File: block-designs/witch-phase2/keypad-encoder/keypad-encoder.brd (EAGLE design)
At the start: 160 x 100 mm, 70 parts, among them IC1 74AHC1G14DBV, IC2 74AHC1G14DBV, IC3 74AHC1G14DBV, IC4 74AHC1G14DBV, IC5 74AHC1G14DBV

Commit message: completed schematic with basic pcb layout
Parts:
- removed D26, D28, D30, D31, D32, D33, D34: (no value), SparkFun-DiscreteSemi:DIODE-1N4001
- removed JP1: (no value), pinhead:1X18
- added D1, D2: (no value), SparkFun-DiscreteSemi:DIODE-1N4001
- added IC6: 74LVC1G17DBV, 74xx-little-us:SOT23-5
- added IC7: 74LVC1G14DBV, 74xx-little-us:SOT23-5
- added JP2: (no value), pinhead:1X10
- added JP3: (no value), pinhead:1X18
- added R17, R18, R19, R20, R21: 1k, resistor:R0805
- C1, C10, C11, C12, C13, C14, C15, C16, C2, C3, C4, C5, C6, C7, C8, C9: value 10uF -> 0.1uF
- IC1, IC2, IC3, IC4, IC5: value 74AHC1G14DBV -> 74LVC1G17DBV
- R1, R10, R11, R12, R13, R14, R15, R16, R2, R3, R4, R5, R6, R7, R8, R9: value 10k -> 1k
- moved D23 353.3 mm to (139.7, 35.6), turned to 90 degrees
- moved D25 352.2 mm to (129.5, 35.6), turned to 90 degrees
- moved D24 348.5 mm to (143.5, 35.6), turned to 90 degrees
- moved D27 337.5 mm to (88.9, 35.6), turned to 90 degrees
- moved D19 323.8 mm to (99.1, 35.6), turned to 90 degrees
- moved D20 319.8 mm to (102.9, 35.6), turned to 90 degrees
- moved D29 317.3 mm to (8.89, 35.6), turned to 90 degrees
- moved D14 309.0 mm to (113.0, 35.6), turned to 90 degrees
- moved D21 308.1 mm to (48.3, 35.6), turned to 90 degrees
- moved D22 305.2 mm to (52.1, 35.6), turned to 90 degrees
- moved D18 303.5 mm to (62.2, 35.6), turned to 90 degrees
- moved D13 302.6 mm to (109.2, 35.6), turned to 90 degrees
- moved D17 297.4 mm to (58.4, 35.6), turned to 90 degrees
- moved D8 289.8 mm to (123.2, 35.6), turned to 90 degrees
- moved D7 283.5 mm to (119.4, 35.6), turned to 90 degrees
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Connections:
- removed net N$10: JP1.9
- removed net N$11: JP1.10
- removed net N$12: JP1.11
- removed net N$13: JP1.12
- removed net N$14: JP1.13
- removed net N$15: JP1.14
- removed net N$16: JP1.15
- removed net N$17: JP1.16
- removed net N$18: JP1.17
- removed net N$2: JP1.1
- removed net N$20: R1.1, R10.1, R11.1, R12.1, R13.1, R14.1, R15.1, R16.1, R2.1, R3.1, R4.1, R5.1, R6.1, R7.1, R8.1, R9.1
- removed net N$3: JP1.2
- removed net N$31: C11.1, D23.A, D24.A, R11.2
- removed net N$37: D11.C, D13.C, D15.C, D17.C, D19.C, D21.C, D23.C, D25.C, D27.C, D29.C, D3.C, D31.C, D33.C, D5.C, D7.C, D9.C
- removed net N$38: D10.C, D12.C, D14.C, D16.C, D18.C, D20.C, D22.C, D24.C, D26.C, D28.C, D30.C, D32.C, D34.C, D4.C, D6.C, D8.C
- removed net N$4: JP1.3
- removed net N$5: JP1.4
- removed net N$6: JP1.5
- removed net N$7: JP1.6
- removed net N$8: JP1.7
- removed net N$9: JP1.8
- new net !RESET: IC7.4, JP2.8
- new net EXEC: IC6.4, JP2.9
- new net OUT_A: D1.C, D15.C, D17.C, D21.C, D29.C, D3.C, IC1.2, R17.2
- new net OUT_B: D19.C, D22.C, D5.C, D7.C, IC2.2, R18.2
- new net OUT_C: D11.C, D23.C, D25.C, D4.C, D6.C, D9.C, IC3.2, R19.2
- new net OUT_D: D10.C, D13.C, D16.C, D24.C, D8.C, IC4.2, R20.2
- new net OUT_E: D12.C, D14.C, D18.C, D2.C, D20.C, D27.C, IC5.2, R21.2
- new net SIGA: IC1.4, JP2.2
- new net SIGB: IC2.4, JP2.3
- new net SIGC: IC3.4, JP2.4
- new net SIGD: IC4.4, JP2.5
- new net SIGE: IC5.4, JP2.6
- new net SW-EXEC: JP3.15, R15.1
- new net SW-MINUS: JP3.10, R13.1
- new net SW-ORDER: JP3.17, R11.1
- new net SW-PLUS: JP3.2, R14.1
- new net SW-RESET: JP3.14, R16.1
- new net SW-SPACE: JP3.16, R12.1
- new net SW0: JP3.6, R10.1
- new net SW1: JP3.5, R6.1
- new net SW2: JP3.9, R1.1
- new net SW3: JP3.13, R2.1
- new net SW4: JP3.4, R3.1
- new net SW5: JP3.8, R4.1
- new net SW6: JP3.12, R5.1
- new net SW7: JP3.3, R7.1
- new net SW8: JP3.7, R8.1
- new net SW9: JP3.11, R9.1
- net GND: now also IC6.3, IC7.3, JP2.10, JP3.18, R17.1, R18.1, R19.1, R20.1, R21.1
- net N$1: now also C11.1, D1.A, D2.A, D23.A, D24.A, R11.2; no longer JP1.18
- net N$32: no longer D26.A
- net N$33: no longer D28.A
- net N$34: no longer D30.A
- net N$35: now also IC6.2; no longer D31.A, D32.A
- net N$36: now also IC7.2; no longer D33.A, D34.A
- net VCC: now also IC6.5, IC7.5, JP2.1, JP3.1
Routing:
- net N$1: track 0.00 -> 19.4 mm
- net N$30: track 0.00 -> 11.8 mm
- net N$29: track 0.00 -> 11.8 mm
- net N$26: track 0.00 -> 11.8 mm
- net N$25: track 0.00 -> 11.8 mm
- net N$23: track 0.00 -> 11.8 mm
- net N$22: track 0.00 -> 11.8 mm
- net N$27: track 0.00 -> 11.7 mm
- net N$24: track 0.00 -> 11.7 mm
- net N$28: track 0.00 -> 11.7 mm
- net N$19: track 0.00 -> 11.7 mm
- net N$36: track 0.00 -> 11.7 mm
- net N$35: track 0.00 -> 11.7 mm
- net N$32: track 0.00 -> 7.94 mm
- net N$34: track 0.00 -> 7.94 mm
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- added copper zone on layer 1, net GND
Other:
- board size 160 x 100 mm -> 159.8 x 99.8 mm

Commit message: layout cleanup
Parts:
- moved IC1 8.13 mm to (53.3, 77.0)
- moved IC2 8.13 mm to (62.2, 77.0)
- moved IC3 8.13 mm to (71.1, 77.0)
- moved IC4 8.13 mm to (80.0, 77.0)
- moved IC5 8.13 mm to (88.9, 77.0)
- moved IC6 8.13 mm to (106.7, 77.0)
- moved IC7 8.13 mm to (97.8, 77.0)
- moved R17 8.13 mm to (52.1, 69.3)
- moved R18 8.13 mm to (61.0, 69.3)
- moved R19 8.13 mm to (69.8, 69.3)
- moved R20 8.13 mm to (78.7, 69.3)
- moved R21 8.13 mm to (87.6, 69.3)
- moved C15 5.59 mm to (110.5, 69.3)
- moved C16 5.59 mm to (101.6, 69.3)
- moved R15 5.59 mm to (106.7, 69.3)
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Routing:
- net OUT_A: track 6.46 -> 243.1 mm, vias 0 -> 7
- net OUT_D: track 6.46 -> 205.4 mm, vias 0 -> 6
- net OUT_C: track 6.46 -> 201.1 mm, vias 0 -> 7
- net OUT_E: track 6.46 -> 162.0 mm, vias 0 -> 6
- net OUT_B: track 6.46 -> 128.2 mm, vias 0 -> 5
- net SW-PLUS: track 0.00 -> 75.5 mm
- net SW-EXEC: track 0.00 -> 73.7 mm, vias 0 -> 1
- net SW7: track 0.00 -> 68.2 mm
- net SW-RESET: track 0.00 -> 67.8 mm, vias 0 -> 1
- net SW-ORDER: track 0.00 -> 63.1 mm
- net SW4: track 0.00 -> 60.3 mm
- net SW-SPACE: track 0.00 -> 55.6 mm
- net SW3: track 0.00 -> 53.1 mm
- net SW1: track 0.00 -> 52.8 mm
- net SW0: track 0.00 -> 44.8 mm
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- added copper zone on layer 16, net VCC

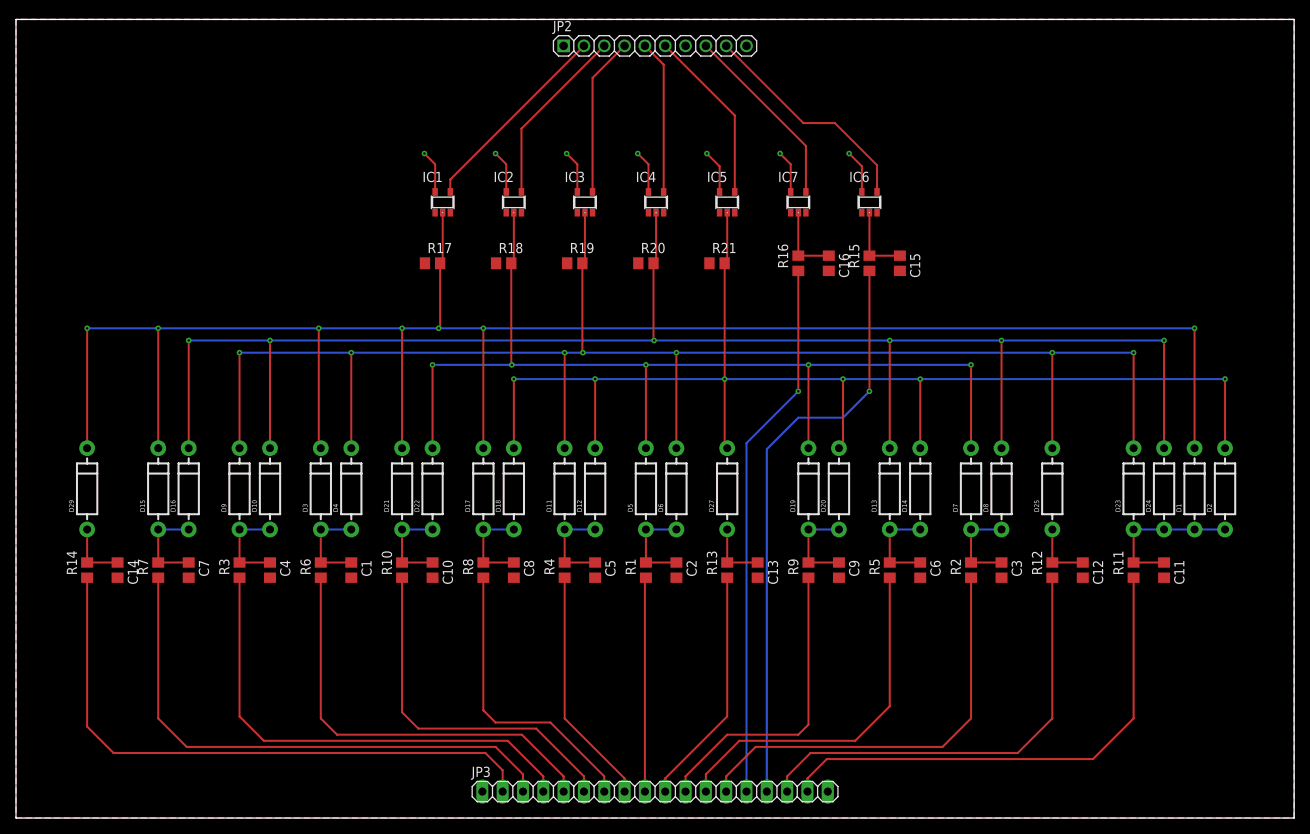
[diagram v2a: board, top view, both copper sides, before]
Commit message: reduced size of module and layout cleanup
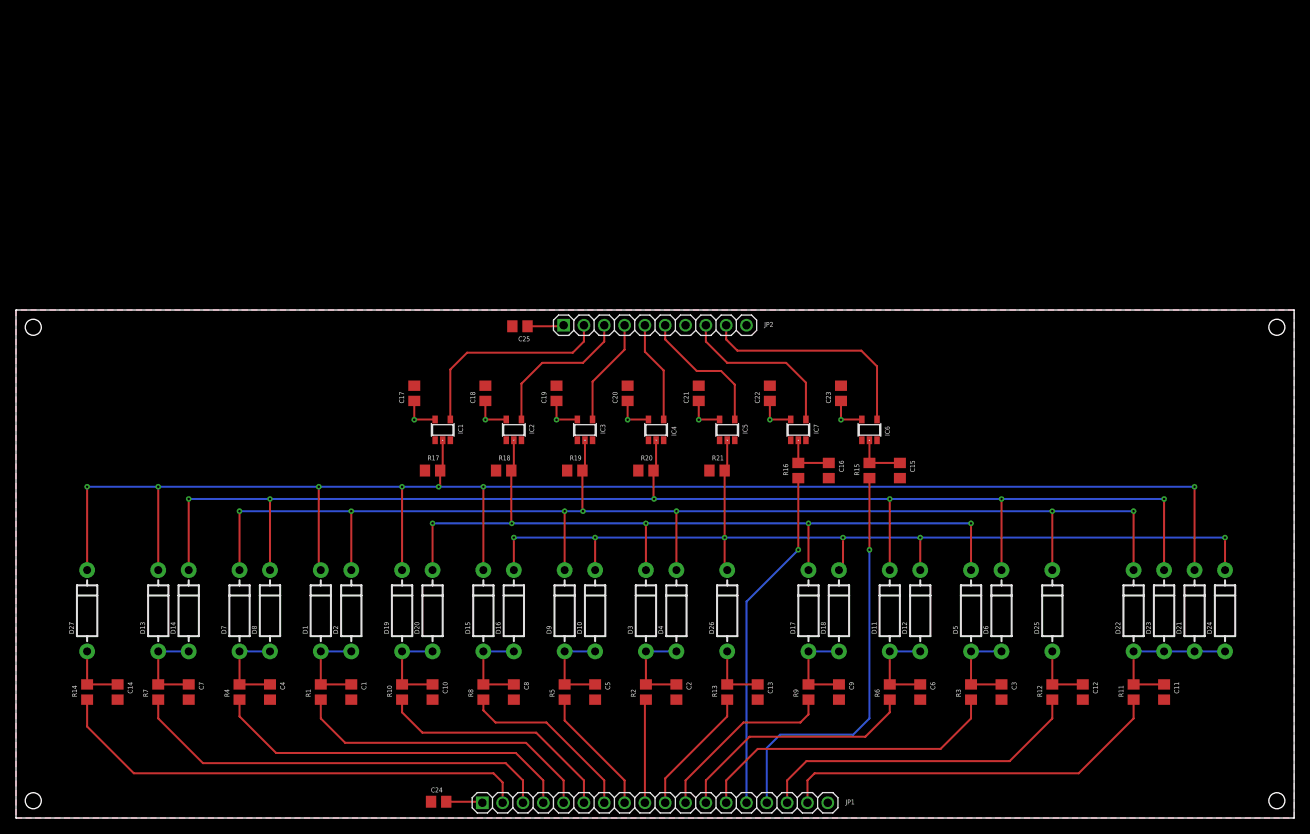
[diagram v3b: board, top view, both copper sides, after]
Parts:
- removed D29: (no value), SparkFun-DiscreteSemi:DIODE-1N4001
- removed JP3: (no value), pinhead:1X18
- added C17, C18, C19, C20, C21, C22, C23: 0.1uF, resistor:C0805
- added C24: 1uF, resistor:C0805
- added C25: 10uF, resistor:C0805
- added D26: (no value), SparkFun-DiscreteSemi:DIODE-1N4001
- added JP1: (no value), pinhead:1X18
- moved D1 110.3 mm to (38.1, 25.9)
- moved D2 110.3 mm to (41.9, 25.9)
- moved D21 100.2 mm to (147.3, 25.9)
- moved D13 92.7 mm to (17.8, 25.9)
- moved D14 92.7 mm to (21.6, 25.9)
- moved D7 92.7 mm to (27.9, 25.9)
- moved D8 92.7 mm to (31.8, 25.9)
- moved R3 92.7 mm to (119.4, 15.7)
- moved D22 88.9 mm to (139.7, 25.9)
- moved D27 81.4 mm to (8.89, 25.9)
- moved R6 72.7 mm to (109.2, 15.7)
- moved D19 53.0 mm to (48.3, 25.9)
- moved D20 53.0 mm to (52.1, 25.9)
- moved D18 43.4 mm to (102.9, 25.9)
- moved D10 43.4 mm to (72.4, 25.9)
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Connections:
- net GND: now also C17.2, C18.2, C19.2, C20.2, C21.2, C22.2, C23.2, C24.2, C25.2, JP1.18; no longer JP3.18
- net N$1: now also D21.A, D22.A; no longer D1.A, D2.A
- net N$19: now also D1.A, D2.A, R1.2; no longer D3.A, D4.A, R6.2
- net N$22: now also D3.A, D4.A, R2.2; no longer D5.A, D6.A, R1.2
- net N$23: now also D5.A, D6.A, R3.2; no longer D7.A, D8.A, R2.2
- net N$24: now also D7.A, D8.A, R4.2; no longer D10.A, D9.A, R3.2
- net N$25: now also D10.A, D9.A, R5.2; no longer D11.A, D12.A, R4.2
- net N$26: now also D11.A, D12.A, R6.2; no longer D13.A, D14.A, R5.2
- net N$27: now also D13.A, D14.A; no longer D15.A, D16.A
- net N$28: now also D15.A, D16.A; no longer D17.A, D18.A
- net N$29: now also D17.A, D18.A; no longer D19.A, D20.A
- net N$30: now also D19.A, D20.A; no longer D21.A, D22.A
- net N$33: now also D26.A; no longer D27.A
- net N$34: now also D27.A; no longer D29.A
- net OUT_A: now also D13.C, D19.C, D27.C; no longer D17.C, D29.C, D3.C
- net OUT_B: now also D17.C, D20.C, D3.C; no longer D19.C, D22.C, D7.C
- net OUT_C: now also D2.C, D22.C, D7.C; no longer D11.C, D23.C, D6.C
- net OUT_D: now also D11.C, D14.C, D23.C, D6.C; no longer D10.C, D13.C, D16.C, D24.C
- net OUT_E: now also D10.C, D16.C, D24.C, D26.C; no longer D14.C, D2.C, D20.C, D27.C
- net SW-EXEC: now also JP1.15; no longer JP3.15
- net SW-MINUS: now also JP1.10; no longer JP3.10
- net SW-ORDER: now also JP1.17; no longer JP3.17
- net SW-PLUS: now also JP1.2; no longer JP3.2
- net SW-RESET: now also JP1.14; no longer JP3.14
- net SW-SPACE: now also JP1.16; no longer JP3.16
- net SW0: now also JP1.6; no longer JP3.6
- net SW1: now also JP1.5, R1.1; no longer JP3.5, R6.1
- net SW2: now also JP1.9, R2.1; no longer JP3.9, R1.1
- net SW3: now also JP1.13, R3.1; no longer JP3.13, R2.1
- net SW4: now also JP1.4, R4.1; no longer JP3.4, R3.1
- net SW5: now also JP1.8, R5.1; no longer JP3.8, R4.1
- net SW6: now also JP1.12, R6.1; no longer JP3.12, R5.1
- net SW7: now also JP1.3; no longer JP3.3
- net SW8: now also JP1.7; no longer JP3.7
- net SW9: now also JP1.11; no longer JP3.11
- net VCC: now also C17.1, C18.1, C19.1, C20.1, C21.1, C22.1, C23.1, C24.1, C25.1, JP1.1; no longer JP3.1
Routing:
- net OUT_E: track 162.0 -> 125.9 mm
- net OUT_C: track 201.1 -> 165.0 mm
- net OUT_A: track 243.1 -> 207.1 mm
- net OUT_D: track 205.4 -> 173.9 mm
- net OUT_B: track 128.2 -> 101.2 mm
- net SW-RESET: track 67.8 -> 43.3 mm
- net SW-EXEC: track 73.7 -> 51.2 mm
- net SW9: track 38.3 -> 23.4 mm
- net SW-PLUS: track 75.5 -> 60.7 mm
- net SW7: track 68.2 -> 53.9 mm
- net SW8: track 37.0 -> 22.9 mm
- net SW4: track 60.3 -> 46.2 mm
- net SW1: track 52.8 -> 38.7 mm
- net SW-SPACE: track 55.6 -> 41.5 mm
- net SW3: track 53.1 -> 39.0 mm
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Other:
- board size 159.8 x 99.8 mm -> 159.8 x 63.5 mm
- board text added: "Keypad Encoder"
